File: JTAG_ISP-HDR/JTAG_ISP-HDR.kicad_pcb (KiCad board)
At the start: 2 copper layers, 23.1 x 46.1 mm, 9 parts, among them J1 Conn_01x08, J2 Conn_01x08

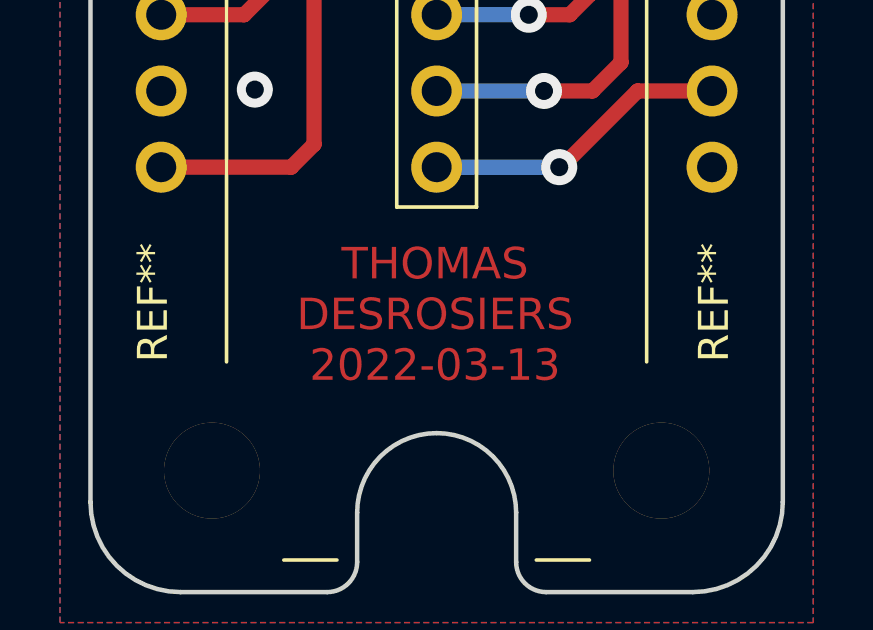
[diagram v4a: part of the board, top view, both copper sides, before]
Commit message: # [PCB] ~ Modification du texte (initiales et date du jours) sur le PCB du projet HDR.
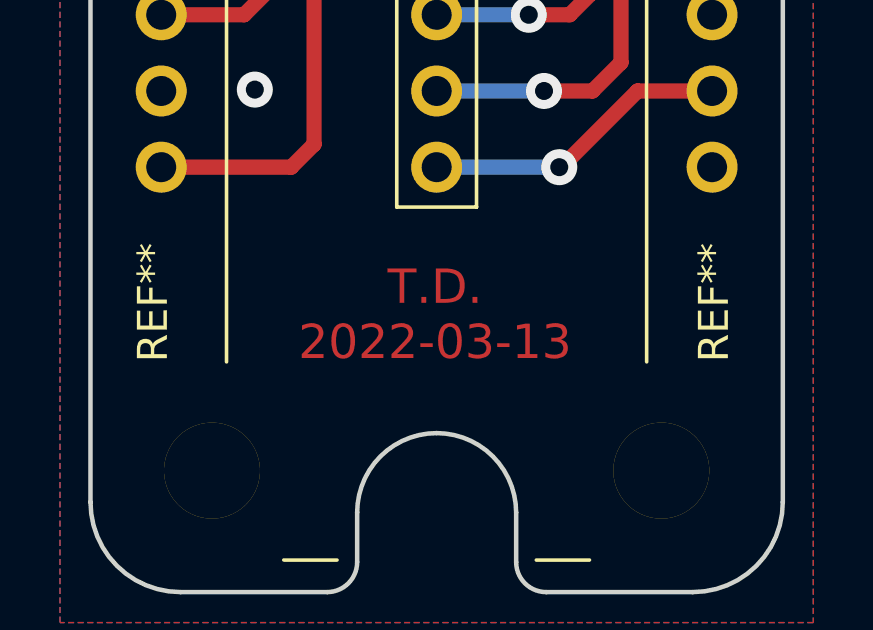
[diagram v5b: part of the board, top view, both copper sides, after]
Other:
- board text added: "T.D. 2022-03-13"
- board text removed: "THOMAS DESROSIERS 2022-03-13"
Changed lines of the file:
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@@
   (gr_line (start 147.822006 107.450001) (end 164.9 107.450001) (layer "User.8") (width 0.15))
   (gr_rect (start 167.9 61.31358) (end 144.822002 107.45) (layer "User.9") (width 0.15) (fill none))
-  (gr_text "THOMAS\nDESROSIERS\n2022-03-13" (at 156.306012 98.197568) (layer "F.Cu")
-    (effects (font (size 1.05 1.05) (thickness 0.15)))
+  (gr_text "T.D.\n2022-03-13" (at 156.306012 98.197568) (layer "F.Cu")
+    (effects (font (size 1.143 1.143) (thickness 0.1905)))
   )
   (segment (start 147.180001 78.04576) (end 152.27424 78.04576) (width 0.508) (layer "F.Cu") (net 1))

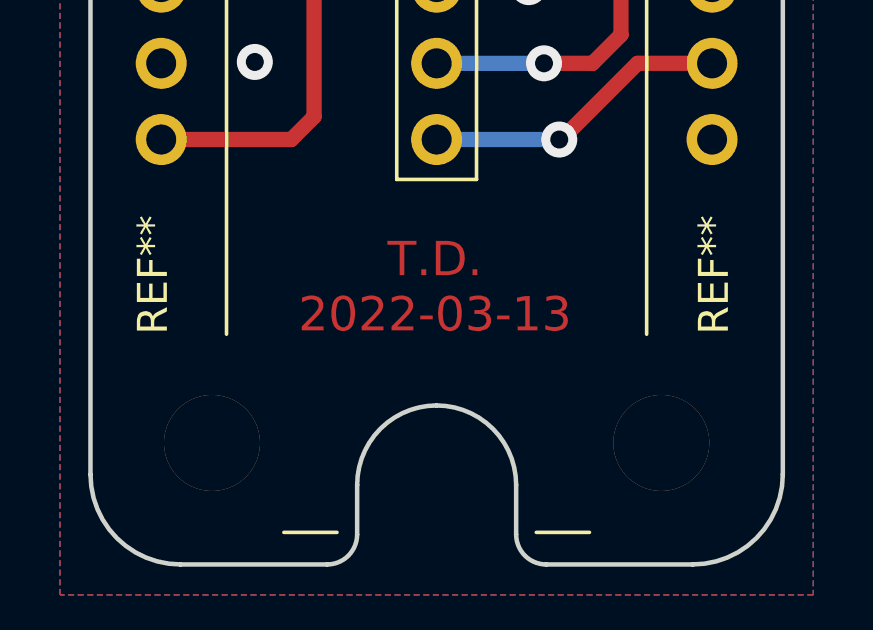
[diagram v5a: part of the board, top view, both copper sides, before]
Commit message: # [PCB] ~ Modification du texte (date du jour) sur le PCB du projet HDR.
# [SCHÉMA]
~ Alignement du texte sur le schéma des 2 projets indiquant le nom des broches sur les headers.
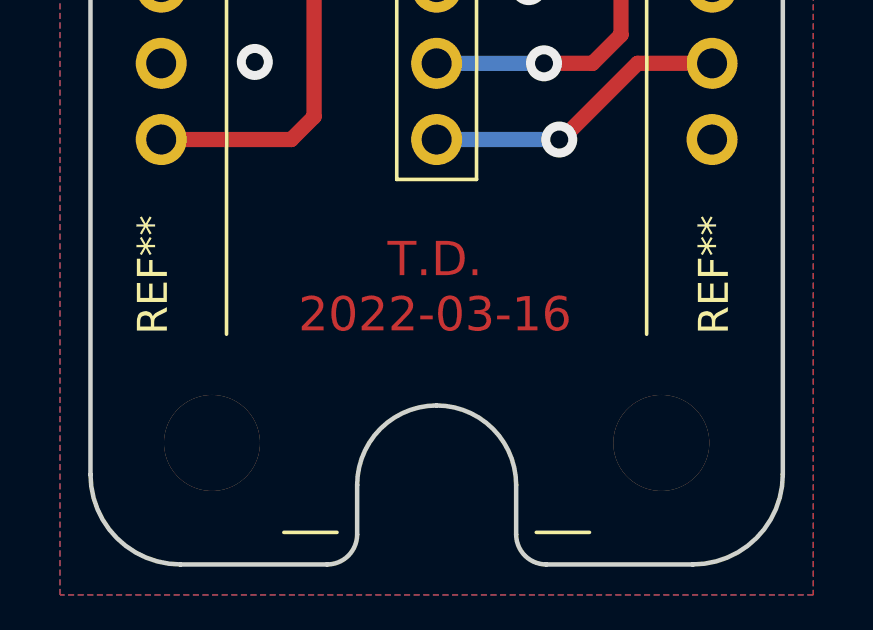
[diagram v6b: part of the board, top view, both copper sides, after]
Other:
- board text added: "T.D. 2022-03-16"
- board text removed: "T.D. 2022-03-13"
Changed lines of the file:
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@@
   (gr_line (start 147.822006 107.450001) (end 164.9 107.450001) (layer "User.8") (width 0.15))
   (gr_rect (start 167.9 61.31358) (end 144.822002 107.45) (layer "User.9") (width 0.15) (fill none))
-  (gr_text "T.D.\n2022-03-13" (at 156.306012 98.197568) (layer "F.Cu")
+  (gr_text "T.D.\n2022-03-16" (at 156.306012 98.197568) (layer "F.Cu")
     (effects (font (size 1.143 1.143) (thickness 0.1905)))
   )

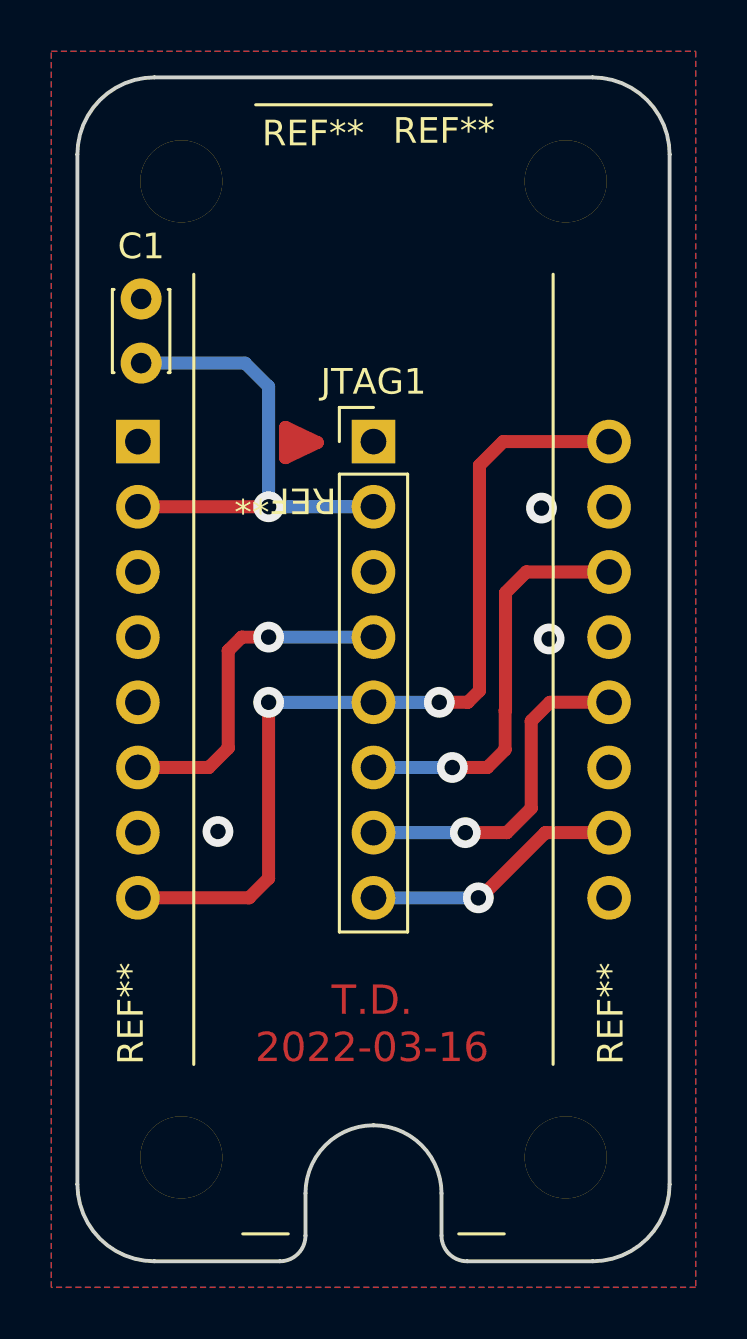
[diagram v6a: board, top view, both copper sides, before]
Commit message: # [PCB] + Ajout d'un trou dans le haut du PCB du projet HDR pour pouvoir y fixer une dragone. ~ Modification de l'empreinte du JTAG. - Non affichage des référence pour les trous et les flèches sur le PCB des 2 projets.
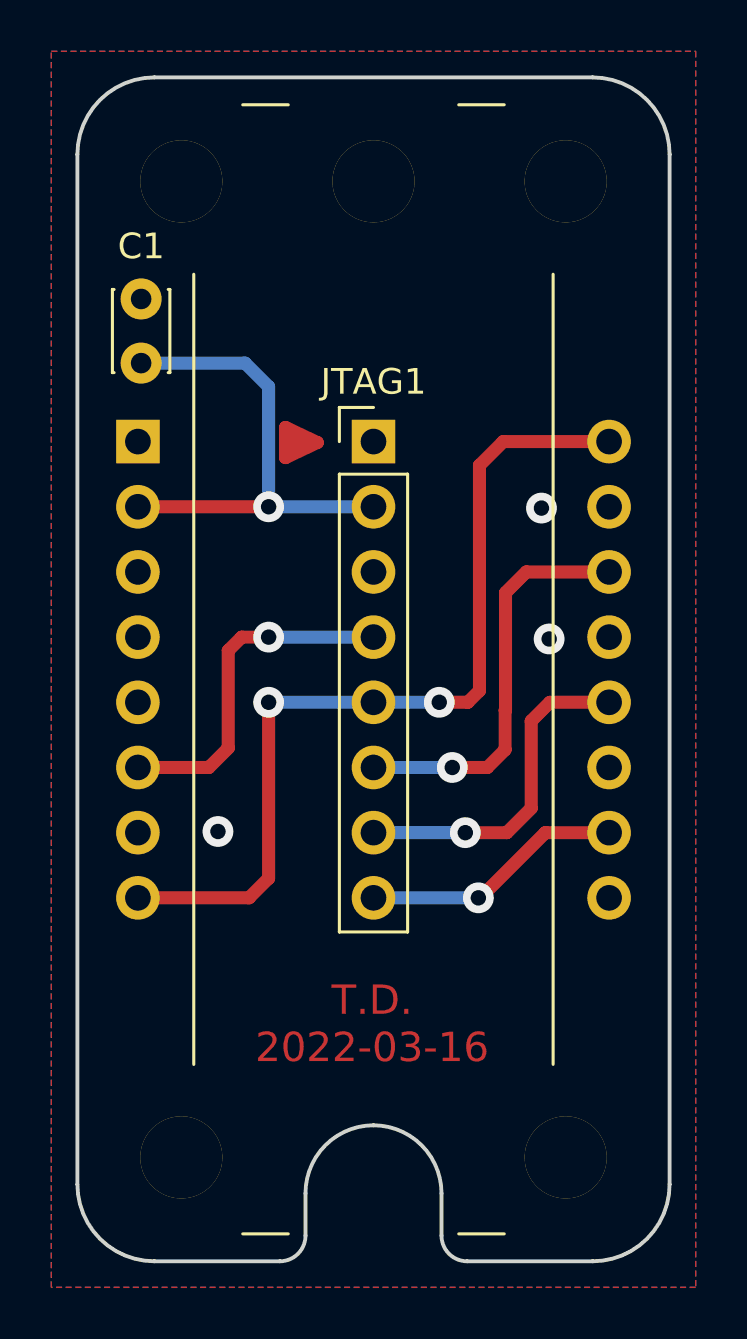
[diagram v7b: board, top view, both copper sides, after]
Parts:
- added REF**: MountingHole_3.2mm_M3, MountingHole:MountingHole_3.2mm_M3, F.Cu at (156.4, 65.4)
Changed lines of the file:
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@@
   (net 16 "unconnected-(JTAG1-Pad1)")
   (footprint "MountingHole:MountingHole_3.2mm_M3" (layer "F.Cu")
+    (at 156.361001 65.36358)
+    (descr "Mounting Hole 3.2mm, no annular, M3")
+    (tags "mounting hole 3.2mm no annular m3")
+    (attr exclude_from_pos_files exclude_from_bom)
+    (fp_text reference "REF**" (at 0.456012 4.833988) (layer "F.SilkS") hide
+      (effects (font (size 1 1) (thickness 0.15)))
+    )
+    (fp_text value "MountingHole_3.2mm_M3" (at 0 4.2) (layer "F.Fab") hide
+      (effects (font (size 1 1) (thickness 0.15)))
+    )
+    (fp_text user "${REFERENCE}" (at 0.456012 4.833988) (layer "F.Fab") hide
+      (effects (font (size 1 1) (thickness 0.15)))
+    )
+    (fp_circle (center 0 0) (end 3.2 0) (layer "Cmts.User") (width 0.15) (fill none))
+    (fp_circle (center 0 0) (end 3.45 0) (layer "F.CrtYd") (width 0.05) (fill none))
+    (pad "" thru_hole circle locked (at 0 0) (size 3.200001 3.200001) (drill 3.200001) (layers *.Cu *.Mask))
+  )
+  (footprint "MountingHole:MountingHole_3.2mm_M3" (layer "F.Cu")
     (at 148.872002 65.36358)
     (descr "Mounting Hole 3.2mm, no annular, M3")
     (tags "mounting hole 3.2mm no annular m3")
     (attr exclude_from_pos_files exclude_from_bom)
-    (fp_text reference "REF**" (at 5.13401 -1.866012) (layer "F.SilkS")
-      (effects (font (size 1 1) (thickness 0.15)))
-    )
-    (fp_text value "MountingHole_3.2mm_M3" (at 0 4.2) (layer "F.Fab") hide
-      (effects (font (size 1 1) (thickness 0.15)))
-    )
-    (fp_text user "${REFERENCE}" (at 5.13401 -1.866012) (layer "F.Fab")
+    (fp_text reference "REF**" (at 2.93401 4.833988) (layer "F.SilkS") hide
+      (effects (font (size 1 1) (thickness 0.15)))
+    )
+    (fp_text value "MountingHole_3.2mm_M3" (at 0 4.2) (layer "F.Fab") hide
+      (effects (font (size 1 1) (thickness 0.15)))
+    )
+    (fp_text user "${REFERENCE}" (at 2.93401 4.833988) (layer "F.Fab") hide
       (effects (font (size 1 1) (thickness 0.15)))
     )
@@
     (at 152.946012 75.897568 180)
     (attr through_hole)
-    (fp_text reference "REF**" (at 0.02 -1.9 180 unlocked) (layer "F.SilkS")
+    (fp_text reference "REF**" (at 0.44 -1.9 180 unlocked) (layer "F.SilkS") hide
       (effects (font (size 1 1) (thickness 0.15)))
     )
@@
       (effects (font (size 1 1) (thickness 0.15)))
     )
-    (fp_text user "${REFERENCE}" (at 0.01 -1.89 180 unlocked) (layer "F.Fab")
+    (fp_text user "${REFERENCE}" (at 0.44 -1.9 180 unlocked) (layer "F.Fab") hide
       (effects (font (size 1 1) (thickness 0.15)))
     )
@@
     (tags "mounting hole 3.2mm no annular m3")
     (attr exclude_from_pos_files exclude_from_bom)
-    (fp_text reference "REF**" (at 1.756012 -5.602432 270) (layer "F.SilkS")
-      (effects (font (size 1 1) (thickness 0.15)))
-    )
-    (fp_text value "MountingHole_3.2mm_M3" (at 0 4.2) (layer "F.Fab") hide
-      (effects (font (size 1 1) (thickness 0.15)))
-    )
-    (fp_text user "${REFERENCE}" (at 1.756012 -5.602432 270) (layer "F.Fab")
+    (fp_text reference "REF**" (at 1.756012 -5.602432 270) (layer "F.SilkS") hide
+      (effects (font (size 1 1) (thickness 0.15)))
+    )
+    (fp_text value "MountingHole_3.2mm_M3" (at 0 4.2) (layer "F.Fab") hide
+      (effects (font (size 1 1) (thickness 0.15)))
+    )
+    (fp_text user "${REFERENCE}" (at 1.756012 -5.602432 270) (layer "F.Fab") hide
       (effects (font (size 1 1) (thickness 0.15)))
     )
@@
     (tags "mounting hole 3.2mm no annular m3")
     (attr exclude_from_pos_files exclude_from_bom)
-    (fp_text reference "REF**" (at -1.96599 -5.602432 90) (layer "F.SilkS")
-      (effects (font (size 1 1) (thickness 0.15)))
-    )
-    (fp_text value "MountingHole_3.2mm_M3" (at 0 4.2) (layer "F.Fab") hide
-      (effects (font (size 1 1) (thickness 0.15)))
-    )
-    (fp_text user "${REFERENCE}" (at -1.96599 -5.602432 90) (layer "F.Fab")
+    (fp_text reference "REF**" (at -1.96599 -5.602432 90) (layer "F.SilkS") hide
+      (effects (font (size 1 1) (thickness 0.15)))
+    )
+    (fp_text value "MountingHole_3.2mm_M3" (at 0 4.2) (layer "F.Fab") hide
+      (effects (font (size 1 1) (thickness 0.15)))
+    )
+    (fp_text user "${REFERENCE}" (at -1.96599 -5.602432 90) (layer "F.Fab") hide
       (effects (font (size 1 1) (thickness 0.15)))
     )
@@
       (effects (font (size 1 1) (thickness 0.15)))
     )
-    (fp_line (start 4.591065 -13.125) (end -4.591065 -13.125) (layer "F.SilkS") (width 0.12))
+    (fp_line (start -3.321065 -13.125) (end -5.095001 -13.125) (layer "F.SilkS") (width 0.12))
     (fp_line (start -1.33 -1.33) (end 0 -1.33) (layer "F.SilkS") (width 0.12))
     (fp_line (start 5.095001 30.874995) (end 3.321065 30.874995) (layer "F.SilkS") (width 0.12))
+    (fp_line (start 5.095001 -13.125) (end 3.321065 -13.125) (layer "F.SilkS") (width 0.12))
     (fp_line (start -7.004065 -6.521) (end -7.004065 24.270995) (layer "F.SilkS") (width 0.12))
     (fp_line (start -1.33 19.11) (end 1.33 19.11) (layer "F.SilkS") (width 0.12))
@@
     (tags "mounting hole 3.2mm no annular m3")
     (attr exclude_from_pos_files exclude_from_bom)
-    (fp_text reference "REF**" (at -4.743988 -1.966012) (layer "F.SilkS")
-      (effects (font (size 1 1) (thickness 0.15)))
-    )
-    (fp_text value "MountingHole_3.2mm_M3" (at 0 4.2) (layer "F.Fab") hide
-      (effects (font (size 1 1) (thickness 0.15)))
-    )
-    (fp_text user "${REFERENCE}" (at -4.743988 -1.966012) (layer "F.Fab")
-      (effects (font (size 1 1) (thickness 0.15)))
-    )
+    (fp_text reference "REF**" (at 1.756012 4.633988) (layer "F.SilkS") hide
+      (effects (font (size 1 1) (thickness 0.15)))
+    )
+    (fp_text value "MountingHole_3.2mm_M3" (at 0 4.2) (layer "F.Fab") hide
+      (effects (font (size 1 1) (thickness 0.15)))
+    )
+    (fp_text user "${REFERENCE}" (at 1.756012 4.633988) (layer "F.Fab") hide
+      (effects (font (size 1 1) (thickness 0.15)))
+    )

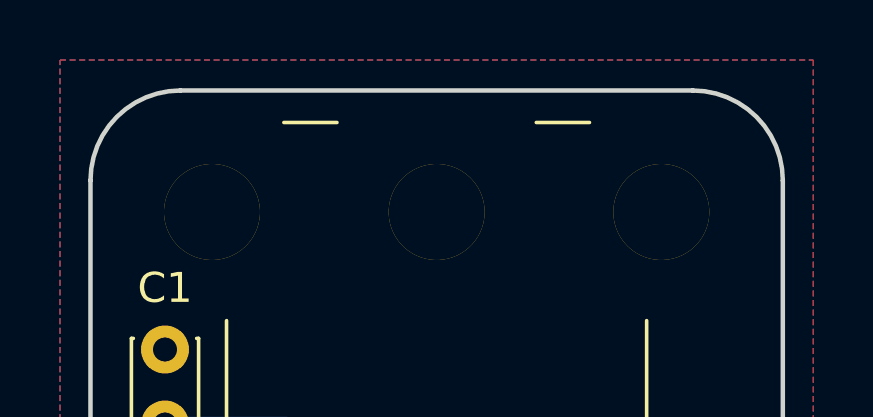
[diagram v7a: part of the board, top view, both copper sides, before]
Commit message: # [PCB] + Ajout d'un encavure dans le haut du PCB du projet HDR pour que la dragone ne dépasse pas sur le bord du PCB. - Suppression du fichier .round-tracks-config qui est inutile. * Mise à jours de la cartouche pour les 2 projets.     * Date actuelle.     * Version actuelle.     * Titre du projet.
# [SCHÉMA]
* Mise à jours de la cartouche pour les 2 projets.
    * Date actuelle.
    * Version actuelle.
    * Titre du projet.
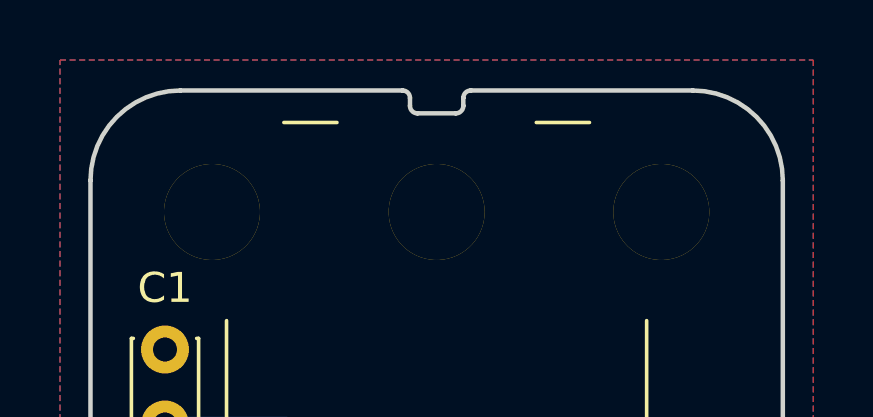
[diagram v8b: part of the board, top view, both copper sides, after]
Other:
- outline, holes or cut-outs redrawn
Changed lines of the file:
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@@
   (paper "A4")
   (title_block
-    (title "JTAG_ISP")
-    (date "2022-03-12")
-    (rev "v1.0.0")
+    (title "JTAG_ISP / HDR")
+    (date "2022-03-17")
+    (rev "v4.1.0")
   )
   (layers
@@
     )
   )
+  (gr_line (start 155.221994 61.31358) (end 147.822002 61.31358) (layer "Edge.Cuts") (width 0.15))
+  (gr_arc (start 157.250012 61.825591) (mid 157.176789 62.002368) (end 157.000012 62.075591) (layer "Edge.Cuts") (width 0.15))
   (gr_line (start 153.710992 104.800011) (end 153.710992 106.45) (layer "Edge.Cuts") (width 0.15))
   (gr_arc (start 167.9 104.45) (mid 167.02132 106.57132) (end 164.9 107.45) (layer "Edge.Cuts") (width 0.15))
+  (gr_line (start 157.250012 61.825591) (end 157.250012 61.563591) (layer "Edge.Cuts") (width 0.15))
+  (gr_line (start 164.900009 61.313591) (end 157.500012 61.313591) (layer "Edge.Cuts") (width 0.15))
   (gr_line (start 164.899997 107.45) (end 160.010981 107.45) (layer "Edge.Cuts") (width 0.15))
   (gr_arc (start 153.710992 104.800011) (mid 154.487159 102.926178) (end 156.360992 102.150011) (layer "Edge.Cuts") (width 0.15))
   (gr_line (start 167.9 104.45) (end 167.9 64.31358) (layer "Edge.Cuts") (width 0.15))
   (gr_arc (start 144.822002 64.31358) (mid 145.700682 62.19226) (end 147.822002 61.31358) (layer "Edge.Cuts") (width 0.15))
-  (gr_line (start 164.9 61.31358) (end 147.822002 61.31358) (layer "Edge.Cuts") (width 0.15))
   (gr_arc (start 156.360981 102.150011) (mid 158.234814 102.926178) (end 159.010981 104.800011) (layer "Edge.Cuts") (width 0.15))
   (gr_arc (start 164.9 61.31358) (mid 167.02132 62.19226) (end 167.9 64.31358) (layer "Edge.Cuts") (width 0.15))
   (gr_line (start 159.010981 106.45) (end 159.010981 104.800011) (layer "Edge.Cuts") (width 0.15))
   (gr_line (start 152.710992 107.45) (end 147.822002 107.45) (layer "Edge.Cuts") (width 0.15))
+  (gr_arc (start 155.221994 61.31358) (mid 155.398772 61.386804) (end 155.471995 61.563583) (layer "Edge.Cuts") (width 0.15))
   (gr_arc (start 160.010981 107.45) (mid 159.303874 107.157107) (end 159.010981 106.45) (layer "Edge.Cuts") (width 0.15))
   (gr_arc (start 153.710992 106.45) (mid 153.418099 107.157107) (end 152.710992 107.45) (layer "Edge.Cuts") (width 0.15))
+  (gr_arc (start 155.721989 62.075591) (mid 155.545212 62.002367) (end 155.47199 61.825588) (layer "Edge.Cuts") (width 0.15))
+  (gr_arc (start 157.250012 61.563591) (mid 157.323235 61.386814) (end 157.500012 61.313591) (layer "Edge.Cuts") (width 0.15))
   (gr_arc (start 147.822002 107.45) (mid 145.700682 106.57132) (end 144.822002 104.45) (layer "Edge.Cuts") (width 0.15))
+  (gr_line (start 157.000012 62.075591) (end 155.721989 62.075591) (layer "Edge.Cuts") (width 0.15))
   (gr_line (start 144.822002 64.31358) (end 144.822002 104.45) (layer "Edge.Cuts") (width 0.15))
+  (gr_line (start 155.471989 61.825587) (end 155.471994 61.563584) (layer "Edge.Cuts") (width 0.15))
   (gr_rect (start 167.899994 61.313568) (end 144.822012 107.450001) (layer "User.1") (width 1.016) (fill none))
   (gr_rect (start 143.806012 60.297568) (end 168.915994 108.466001) (layer "User.2") (width 0.15) (fill none))
   (gr_line (start 147.822006 107.450001) (end 164.9 107.450001) (layer "User.8") (width 0.15))
+  (gr_line (start 164.9 61.313568) (end 147.822006 61.313568) (layer "User.8") (width 0.15))
   (gr_rect (start 167.9 61.31358) (end 144.822002 107.45) (layer "User.9") (width 0.15) (fill none))
   (gr_text "T.D.\n2022-03-16" (at 156.306012 98.197568) (layer "F.Cu")
